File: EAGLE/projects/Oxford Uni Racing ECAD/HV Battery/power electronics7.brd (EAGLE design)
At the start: 144.8 x 104.1 mm, 49 parts, among them IC1 4043D, IC2 SE555D, IC6 4011D, K1 T9AS1D12-48=T9A, K2 T9AS5D12-12=T9A, K3 T9AS1D12-48=T9A, K4 T9AS1D12-48=T9A, K5 T9AS1D12-48=T9A, Q1 BSS138, Q2 BSS138, Q3 BSS138

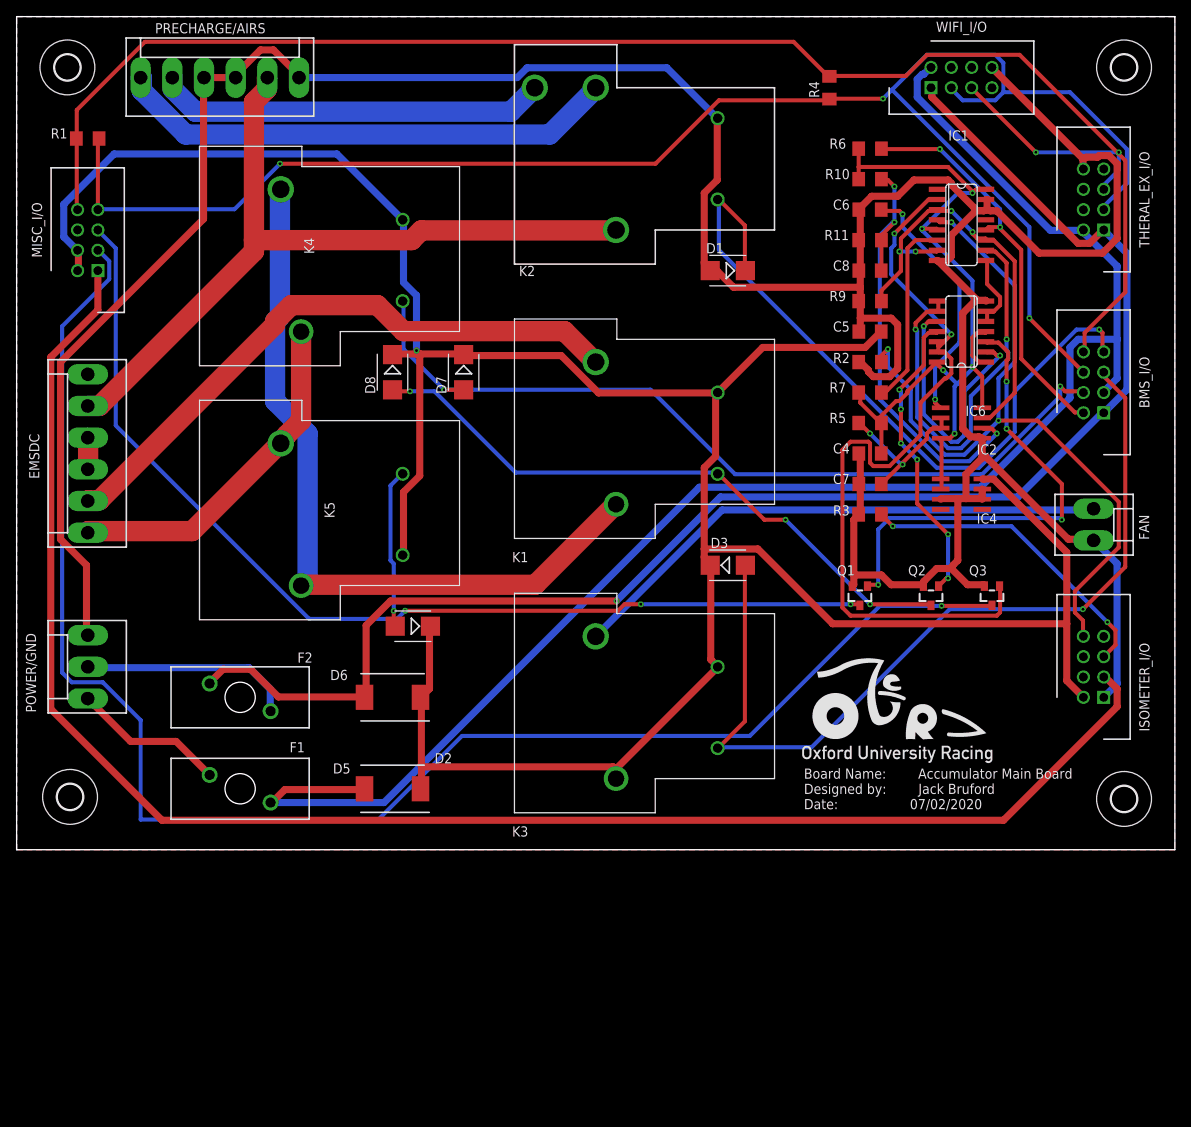
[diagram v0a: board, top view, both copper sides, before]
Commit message: added wills suggestions and test pads
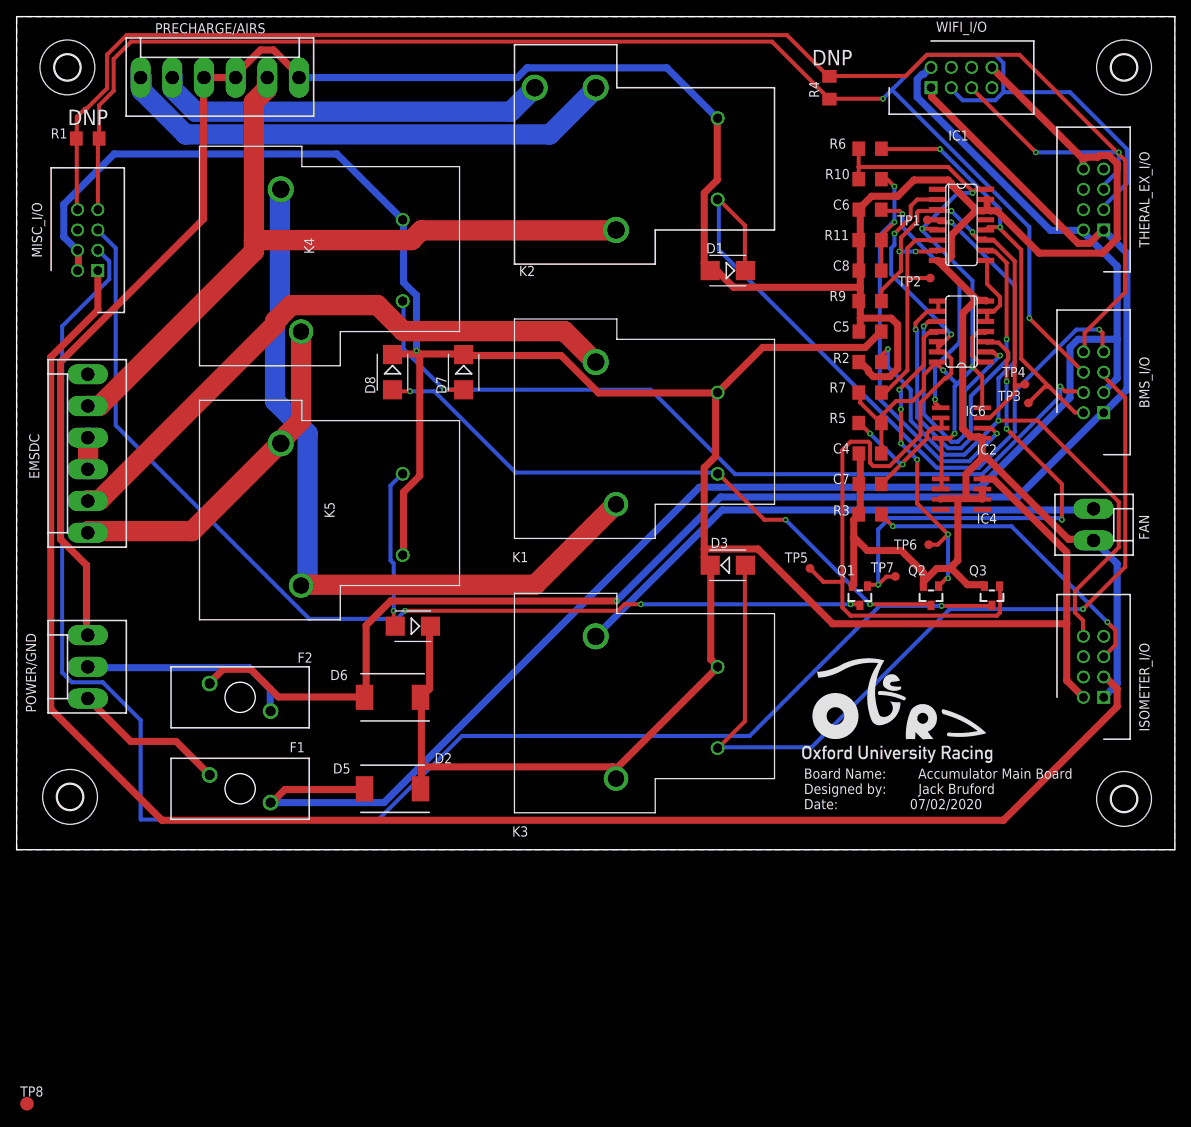
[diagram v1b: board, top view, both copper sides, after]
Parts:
- added TP1, TP2, TP3, TP4, TP5, TP6, TP7: TPSTP11R, testpad:TP11R
- added TP8: TPSTP17R, testpad:TP17R
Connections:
- net CHG_SAFE: now also TP3.TP
- net DISCHARE_ENABLE: now also TP2.TP
- net N$21: now also TP7.TP
- net N$37: now also TP6.TP
- net N$8: now also TP5.TP
- net OK_HS: now also TP1.TP
- net STARTUP_RESET: now also TP4.TP
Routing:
- net CAN2_H: track 214.3 -> 221.2 mm, vias 3 -> 2
- net N$8: track 97.8 -> 103.4 mm
- net CHG_SAFE: track 50.3 -> 53.7 mm
- net N$37: track 37.5 -> 40.4 mm
- net GND: track 430.7 -> 433.7 mm
- net DISCHARE_ENABLE: track 23.8 -> 26.7 mm
- net CAN2_L: track 208.9 -> 211.6 mm
- net N$21: track 59.2 -> 61.7 mm
- net STARTUP_RESET: track 54.3 -> 56.3 mm
- net OK_HS: track 96.2 -> 97.4 mm
- net +3V3: track 98.7 -> 99.6 mm
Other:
- board text added: "DNP"
